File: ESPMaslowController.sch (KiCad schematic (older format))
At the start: 35 parts, among them J1 Barrel_Jack_Switch, J10 Conn_01x08, J2 B6B-PH-SM4-TB, J3 B6B-PH-SM4-TB, J4 B6B-PH-SM4-TB, J5 B6B-PH-SM4-TB, J6 B6B-PH-SM4-TB, J7 Micro_SD_Card_Det, J8 Conn_01x08, J9 Conn_01x08, U1 NCP3063, U2 ESP32_DevKitV1, U3 ATmega328PB-AU

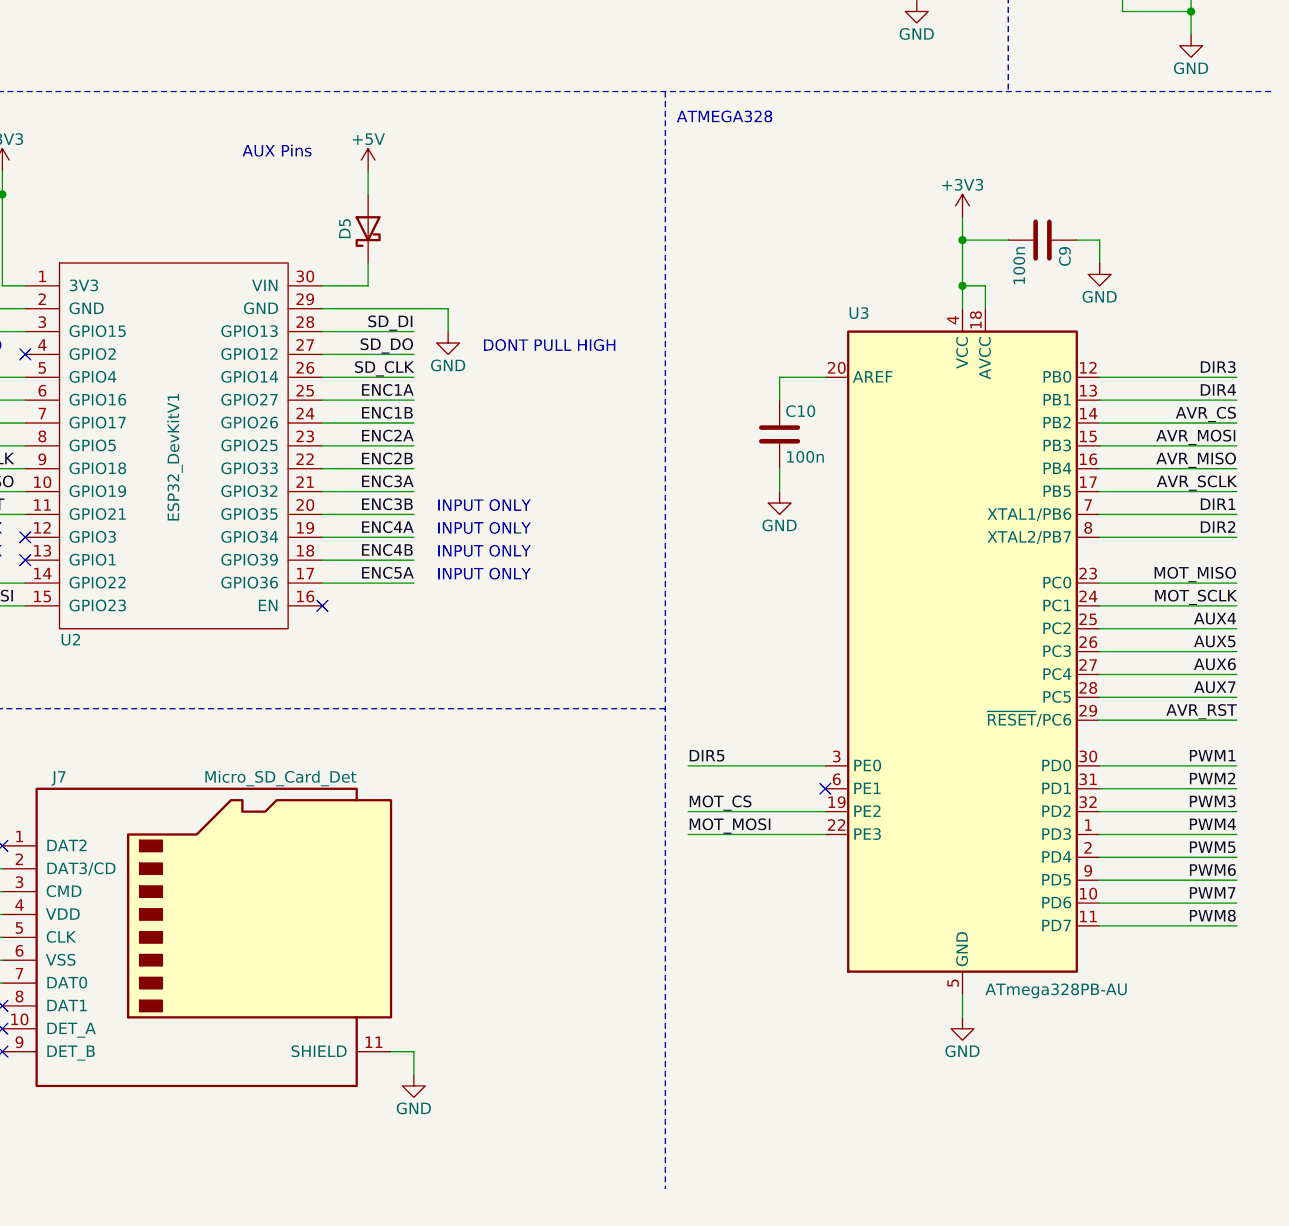
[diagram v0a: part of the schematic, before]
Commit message: Moved PWM outputs to OC pins on ATmega328.
The original plan was to do a software PWM on Port D. Testing showed frequencies of only 450 Hz could be achieved at 100% CPU usage. This is too low to be useful, and was not phase-correct PWM.
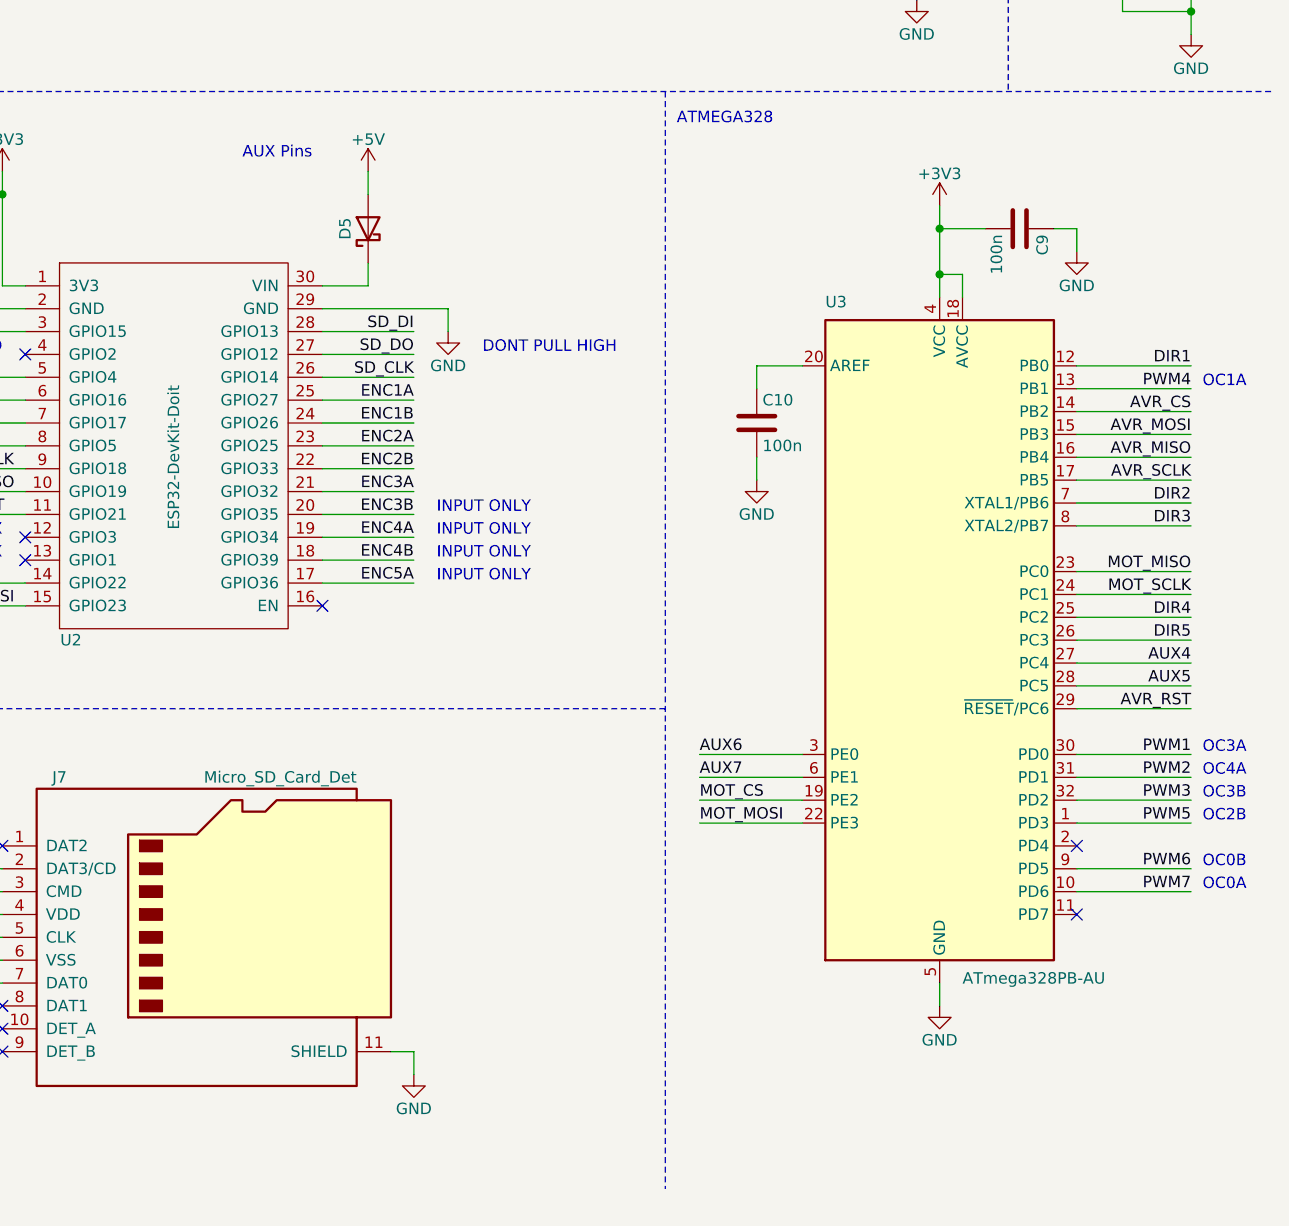
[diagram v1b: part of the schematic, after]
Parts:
- U2: value ESP32_DevKitV1 -> ESP32-DevKit-Doit; BuyLink (none) -> https://www.aliexpress.com/item/4000111107743.html; MFR (none) -> Espressif; MPN (none) -> ESP32-DEVKITC-32D; Price (none) -> 10.00
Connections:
- net AUX4: now also U3.27 (PC4); no longer U3.25 (PC2)
- net AUX5: now also U3.28 (PC5); no longer U3.26 (PC3)
- net AUX6: now also U3.3 (PE0); no longer U3.27 (PC4)
- net AUX7: now also U3.6 (PE1); no longer U3.28 (PC5)
- net DIR1: now also U3.12 (PB0); no longer U3.7 (XTAL1/PB6)
- net DIR2: now also U3.7 (XTAL1/PB6); no longer U3.8 (XTAL2/PB7)
- net DIR3: now also U3.8 (XTAL2/PB7); no longer U3.12 (PB0)
- net DIR4: now also U3.25 (PC2); no longer U3.13 (PB1)
- net DIR5: now also U3.26 (PC3); no longer U3.3 (PE0)
- net PWM4: now also U3.13 (PB1); no longer U3.1 (PD3)
- net PWM5: now also U3.1 (PD3); no longer U3.2 (PD4)
- net PWM8: no longer names the net of U3.11 (PD7)
- no-connect marks 10 -> 11
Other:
- note added: "OC0A"
- note added: "OC0B"
- note added: "OC1A"
- note added: "OC2B"
- note added: "OC3A"
- note added: "OC3B"
- note added: "OC4A"
- moved on the sheet: C10, C9, U3

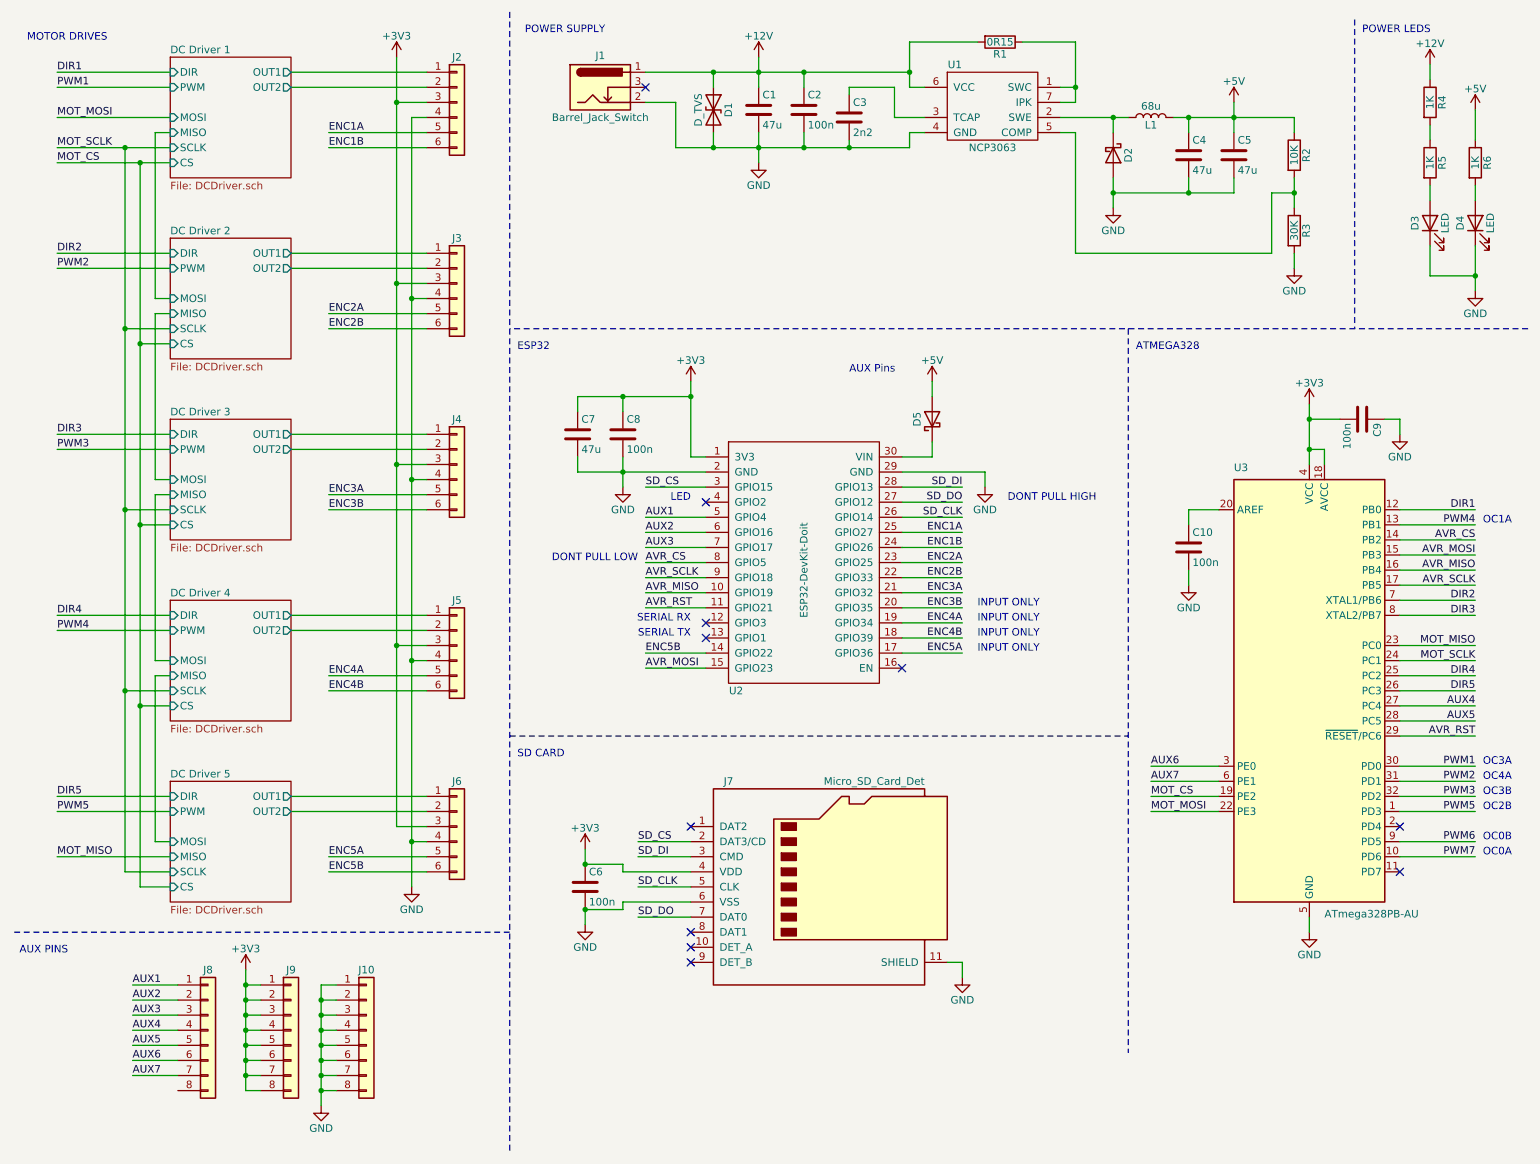
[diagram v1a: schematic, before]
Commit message: Finalized BOM and reworked AUX pins.
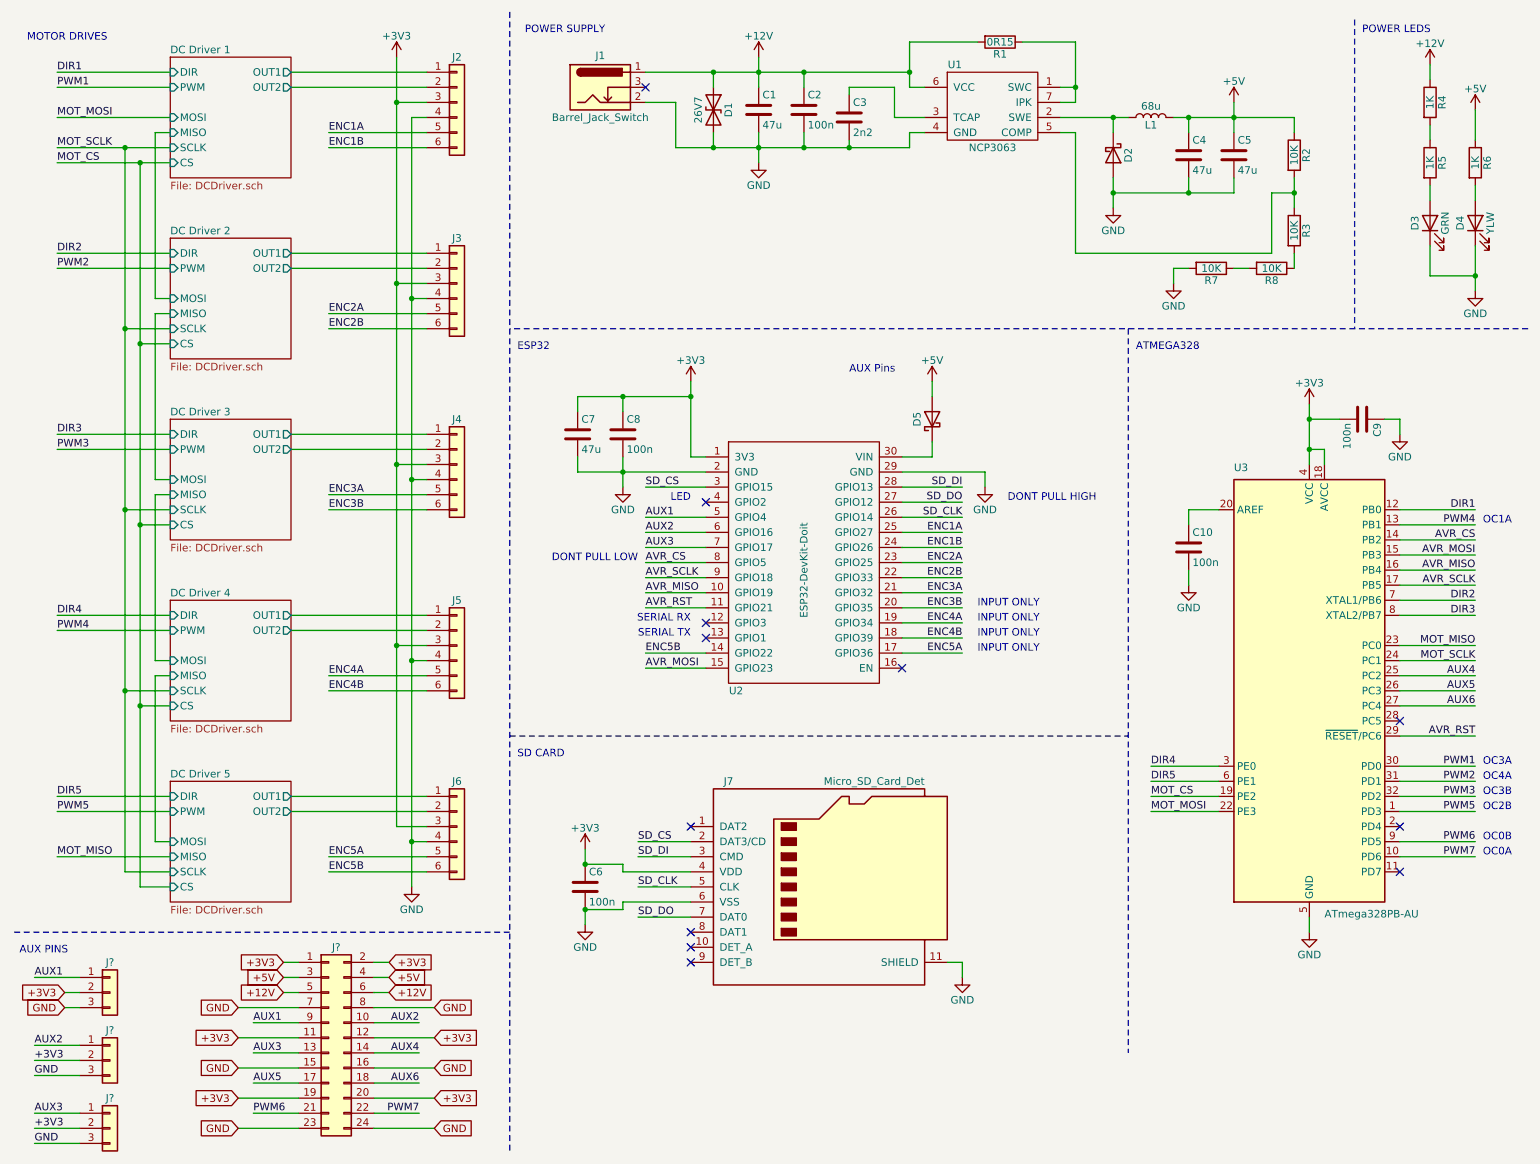
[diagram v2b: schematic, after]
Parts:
- removed J10, J8, J9: Conn_01x08, symbol Connector_Generic:Conn_01x08
- added J?: Conn_02x12_Odd_Even, Connector_PinHeader_2.54mm:PinHeader_2x12_P2.54mm_Vertical, symbol Connector_Generic:Conn_02x12_Odd_Even
- added J? (x3): Conn_01x03, Connector_PinHeader_2.54mm:PinHeader_1x03_P2.54mm_Vertical, symbol Connector_Generic:Conn_01x03
- added R7, R8: 10K, Resistor_SMD:R_0805_2012Metric, symbol Device:R
- D1: value D_TVS -> 26V7
- D3: value LED -> GRN; footprint (none) -> LED_SMD:LED_0805_2012Metric_Castellated; MFR (none) -> Lite-On; MPN (none) -> LTST-C170KGKT; Price (none) -> 0.35
- D4: value LED -> YLW; footprint (none) -> LED_SMD:LED_0805_2012Metric_Castellated; MFR (none) -> Lite-On; MPN (none) -> LTST-C171KSKT; Price (none) -> 0.31
- L1: footprint Inductor_SMD:L_12x12mm_H6mm -> Inductor_SMD:L_12x12mm_H8mm; MFR GLE -> Taiyo Yuden; MPN GCRH125-680MC -> NS12575T680MN
- R1: footprint (none) -> Resistor_SMD:R_1206_3216Metric; MFR (none) -> Yageo; MPN (none) -> RL1206FR-070R15L; Price (none) -> 0.36
- R2: footprint (none) -> Resistor_SMD:R_0805_2012Metric; MFR (none) -> Yageo; MPN (none) -> RC0805FR-0710KL; Price (none) -> 0.10
- R3: value 30K -> 10K; footprint (none) -> Resistor_SMD:R_0805_2012Metric; MFR (none) -> Yageo; MPN (none) -> RC0805FR-0710KL; Price (none) -> 0.10
- R4, R5, R6: footprint (none) -> Resistor_SMD:R_0805_2012Metric; MFR (none) -> Yageo; MPN (none) -> RC0805FR-071KL; Price (none) -> 0.10
- U1: Price (none) -> 0.89
- U2: MPN ESP32-DEVKITC-32D -> ESP32 DevKit v1; Price 10.00 -> 6.00
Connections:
- net AUX7 is gone; now on net DIR5: U3.6 (PE1)
- net +12V: now also J?.5 (Pin_5), J?.6 (Pin_6)
- net +3V3: now also J?.1 (Pin_1), J?.11 (Pin_11), J?.12 (Pin_12), J?.19 (Pin_19), J?.2 (Pin_2), J?.2 (Pin_2), J?.2 (Pin_2), J?.2 (Pin_2), J?.20 (Pin_20)
- net +5V: now also J?.3 (Pin_3), J?.4 (Pin_4)
- net AUX1: now also J?.1 (Pin_1), J?.9 (Pin_9)
- net AUX2: now also J?.1 (Pin_1), J?.10 (Pin_10)
- net AUX3: now also J?.1 (Pin_1), J?.13 (Pin_13)
- net AUX4: now also U3.25 (PC2), J?.14 (Pin_14); no longer U3.27 (PC4)
- net AUX5: now also U3.26 (PC3), J?.17 (Pin_17); no longer U3.28 (PC5)
- net AUX6: now also U3.27 (PC4), J?.18 (Pin_18); no longer U3.3 (PE0)
- net DIR4: now also U3.3 (PE0); no longer U3.25 (PC2)
- net DIR5: no longer U3.26 (PC3)
- net GND: now also J?.15 (Pin_15), J?.16 (Pin_16), J?.23 (Pin_23), J?.24 (Pin_24), J?.3 (Pin_3), J?.3 (Pin_3), J?.3 (Pin_3), J?.7 (Pin_7), J?.8 (Pin_8), R7.2; no longer R3.2
- net PWM6: now also J?.21 (Pin_21)
- net PWM7: now also J?.22 (Pin_22)
- new net: R3.2, R8.1
- new net: R7.1, R8.2
- no-connect marks 11 -> 12

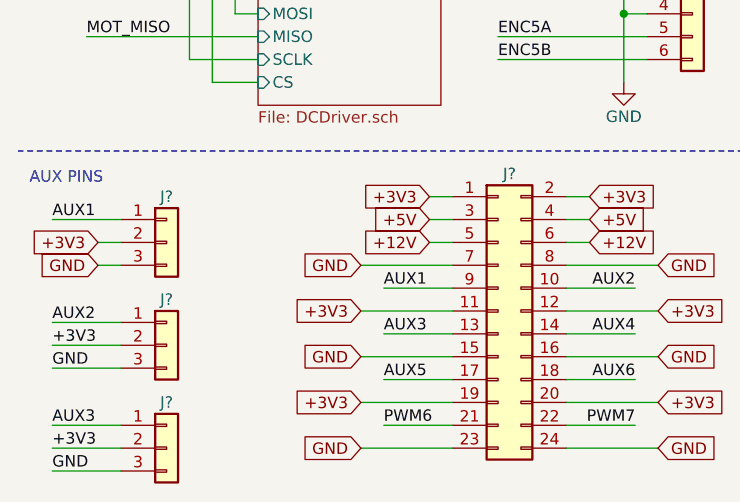
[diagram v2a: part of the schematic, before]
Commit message: Created footprint for ESP32.
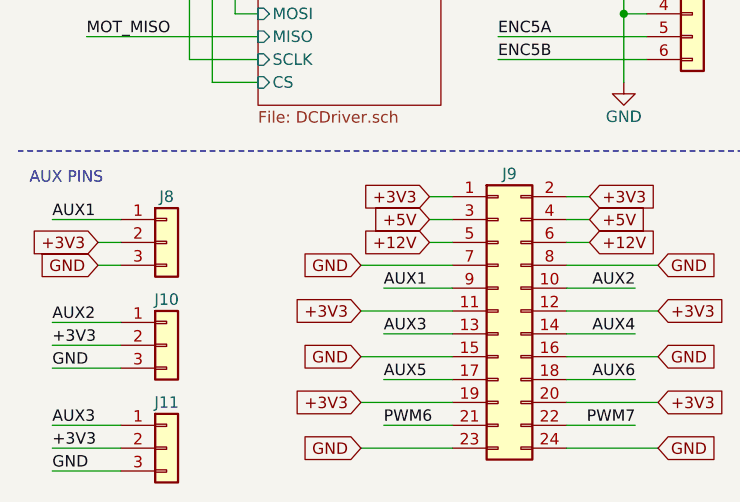
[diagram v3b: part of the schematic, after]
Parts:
- U2: footprint (none) -> ProjectFootprints:ESP32-DEVKIT-V1
- gave numbers to parts that had none: 4
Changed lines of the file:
@@
 F 0 "U2" H 5300 4850 50  0000 C CNN
 F 1 "ESP32-DevKit-Doit" V 5750 5650 50  0000 C CNN
-F 2 "" H 5250 4900 50  0001 C CNN
+F 2 "ProjectFootprints:ESP32-DEVKIT-V1" H 5250 4900 50  0001 C CNN
 F 3 "" H 5250 4900 50  0001 C CNN
 F 4 "6.00" H 5250 4900 50  0001 C CNN "Price"
@@
 NoConn ~ 9700 5150
 $Comp
-L Connector_Generic:Conn_02x12_Odd_Even J?
+L Connector_Generic:Conn_02x12_Odd_Even J9
 U 1 1 5F95DFCD
 P 2600 7250
-F 0 "J?" H 2650 7850 50  0000 C CNN
+F 0 "J9" H 2650 7850 50  0000 C CNN
 F 1 "Conn_02x12_Odd_Even" H 2650 6550 50  0001 C CNN
 F 2 "Connector_PinHeader_2.54mm:PinHeader_2x12_P2.54mm_Vertical" H 2600 7250 50  0001 C CNN
@@
 $EndComp
 $Comp
-L Connector_Generic:Conn_01x03 J?
+L Connector_Generic:Conn_01x03 J8
 U 1 1 5F95F27A
 P 1150 6950
-F 0 "J?" H 1150 7150 50  0000 C CNN
+F 0 "J8" H 1150 7150 50  0000 C CNN
 F 1 "Conn_01x03" H 1150 6750 50  0001 C CNN
 F 2 "Connector_PinHeader_2.54mm:PinHeader_1x03_P2.54mm_Vertical" H 1150 6950 50  0001 C CNN
@@
 	2000 7850 2400 7850
 $Comp
-L Connector_Generic:Conn_01x03 J?
+L Connector_Generic:Conn_01x03 J10
 U 1 1 5FFE5A31
 P 1150 7400
-F 0 "J?" H 1150 7600 50  0000 C CNN
+F 0 "J10" H 1150 7600 50  0000 C CNN
 F 1 "Conn_01x03" H 1150 7200 50  0001 C CNN
 F 2 "Connector_PinHeader_2.54mm:PinHeader_1x03_P2.54mm_Vertical" H 1150 7400 50  0001 C CNN
@@
 $EndComp
 $Comp
-L Connector_Generic:Conn_01x03 J?
+L Connector_Generic:Conn_01x03 J11
 U 1 1 5FFE5EB2
 P 1150 7850
-F 0 "J?" H 1150 8050 50  0000 C CNN
+F 0 "J11" H 1150 8050 50  0000 C CNN
 F 1 "Conn_01x03" H 1150 7650 50  0001 C CNN
 F 2 "Connector_PinHeader_2.54mm:PinHeader_1x03_P2.54mm_Vertical" H 1150 7850 50  0001 C CNN
